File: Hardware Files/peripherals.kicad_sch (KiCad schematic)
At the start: 6 parts, among them J1 Micro_SD_Card_Det1, J2 Conn_ST_STDC14, Y1 16MHz

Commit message: STARTED PCB DESIGN!!
Footprints added to schematic components(some may need to be changed). Organized components and started some rough draft routing. Will most likely need some reorganization, how will parts affect each other(caps, inductors)? NEED TO ADD SOLDER POINTS for battery holder AND FOR 2 other IMUs.
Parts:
- C10, C11: footprint (none) -> Capacitor_SMD:C_Elec_3x5.4
- J1: footprint (none) -> Connector_Card:microSD_HC_Wuerth_693072010801
- J2: footprint (none) -> Connector:Tag-Connect_TC2030-IDC-FP_2x03_P1.27mm_Vertical
- R2: footprint (none) -> Resistor_SMD:R_0201_0603Metric
- Y1: footprint (none) -> Crystal:Crystal_SMD_0603-4Pin_6.0x3.5mm
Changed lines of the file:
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@@
       (effects (font (size 1.27 1.27)) (justify right))
     )
-    (property "Footprint" "" (at 49.53 99.06 0)
+    (property "Footprint" "Connector:Tag-Connect_TC2030-IDC-FP_2x03_P1.27mm_Vertical" (at 49.53 99.06 0)
       (effects (font (size 1.27 1.27)) hide)
     )
@@
       (effects (font (size 1.27 1.27)) (justify left))
     )
-    (property "Footprint" "" (at 53.34 40.64 0)
+    (property "Footprint" "Capacitor_SMD:C_Elec_3x5.4" (at 53.34 40.64 0)
       (effects (font (size 1.27 1.27)) hide)
     )
@@
       (effects (font (size 1.27 1.27)))
     )
-    (property "Footprint" "" (at 64.77 53.34 0)
+    (property "Footprint" "Connector_Card:microSD_HC_Wuerth_693072010801" (at 64.77 53.34 0)
       (effects (font (size 1.27 1.27)) hide)
     )
@@
       (effects (font (size 1.27 1.27)))
     )
-    (property "Footprint" "" (at 43.18 38.1 0)
+    (property "Footprint" "Crystal:Crystal_SMD_0603-4Pin_6.0x3.5mm" (at 43.18 38.1 0)
       (effects (font (size 1.27 1.27)) hide)
     )
@@
       (effects (font (size 1.27 1.27)) (justify left))
     )
-    (property "Footprint" "" (at 53.34 33.02 0)
+    (property "Footprint" "Resistor_SMD:R_0201_0603Metric" (at 53.34 33.02 0)
       (effects (font (size 1.27 1.27)) hide)
     )
@@
       (effects (font (size 1.27 1.27)) (justify left))
     )
-    (property "Footprint" "" (at 33.02 40.64 0)
-      (effects (font (size 1.27 1.27)) hide)
-    )
+    (property "Footprint" "Capacitor_SMD:C_Elec_3x5.4" (at 33.02 40.64 0)
+      (effects (font (size 1.27 1.27)) hide)
+    )

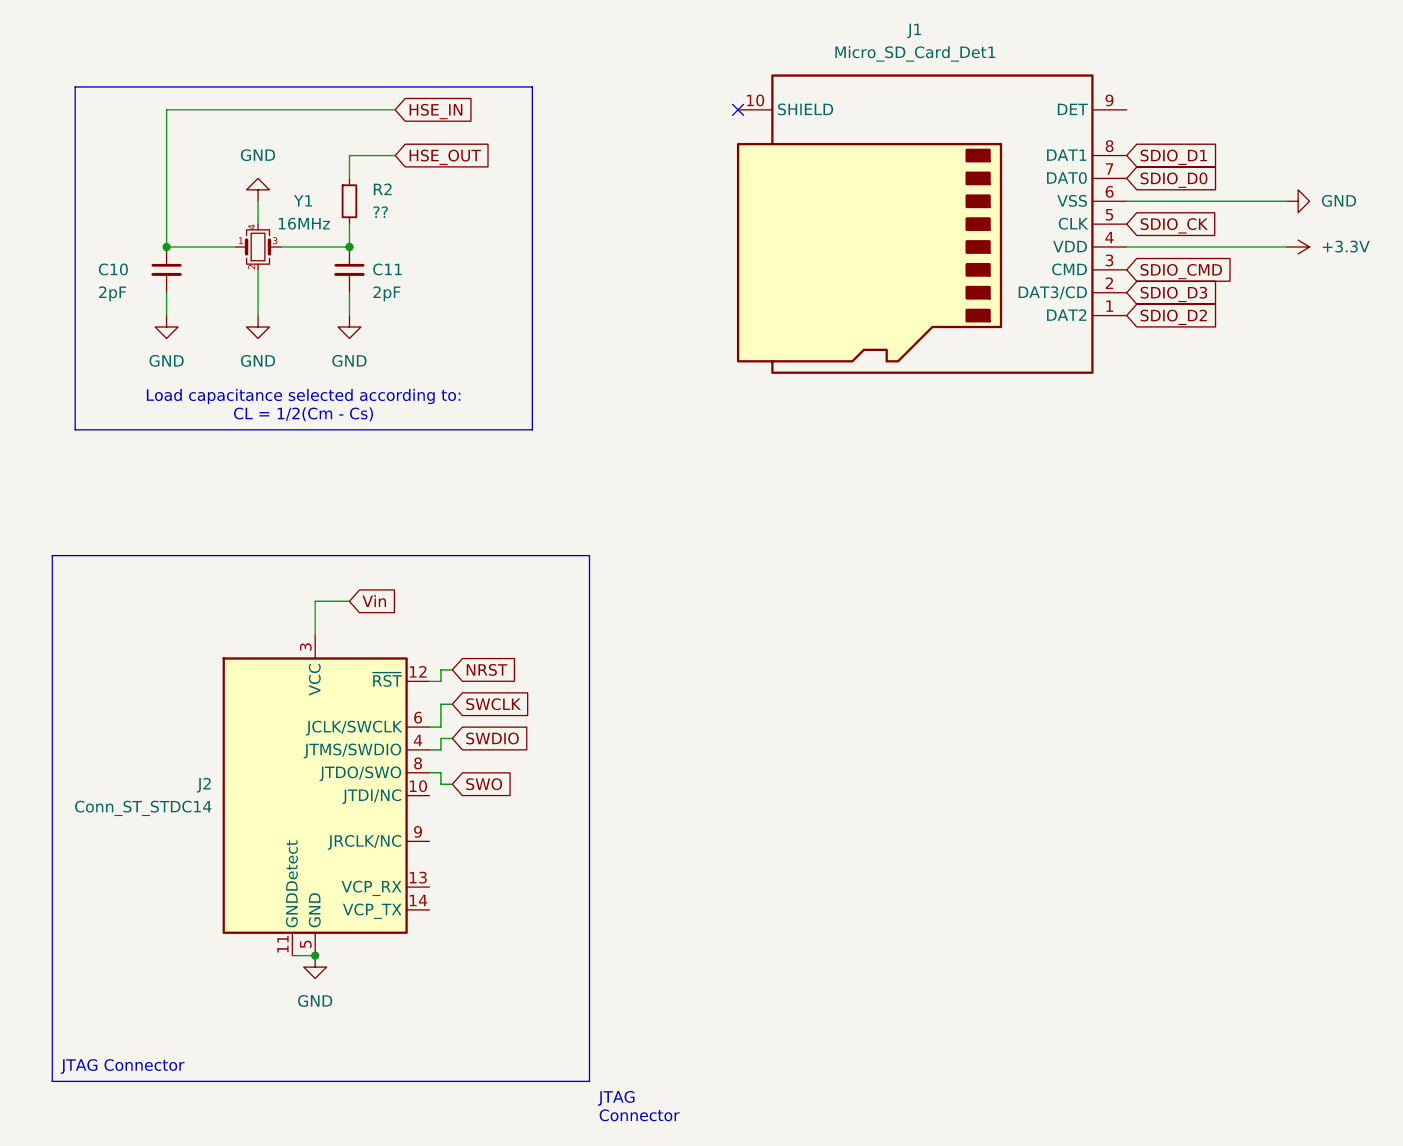
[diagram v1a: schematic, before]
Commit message: Added comments
Added NC flag to the detect pin on SD reader. Left a comment to add NC flags into the MCU for all unused pins.
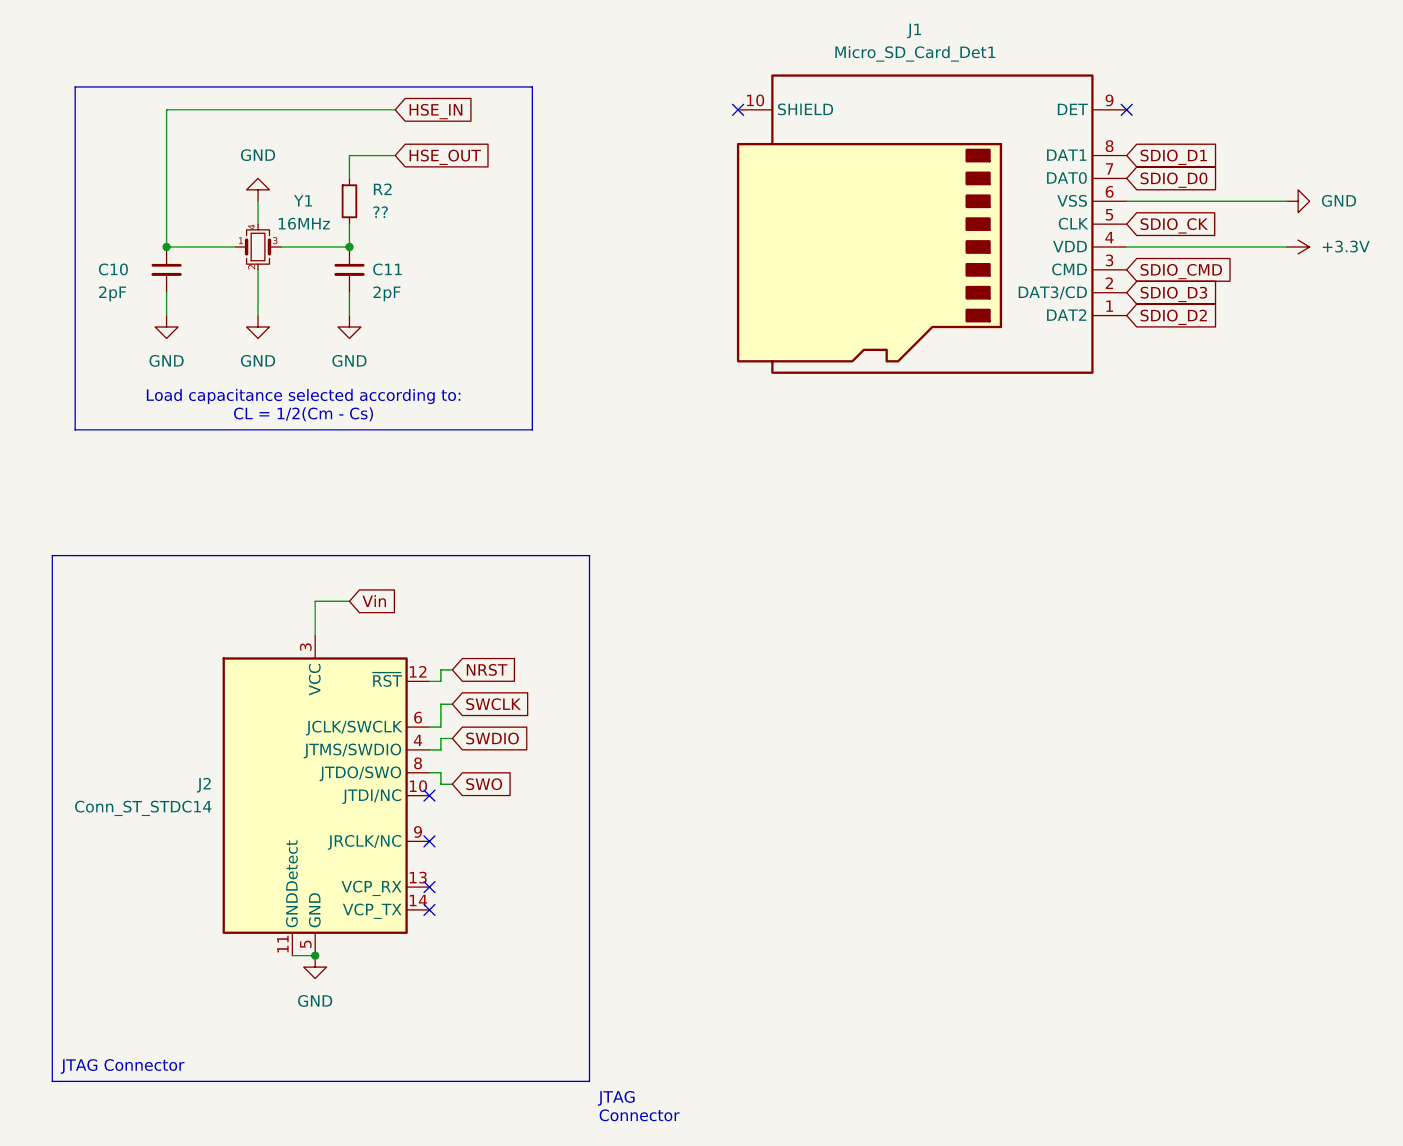
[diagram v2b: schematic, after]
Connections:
- no-connect marks 1 -> 6
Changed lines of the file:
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@@
   )
   (no_connect (at 96.52 22.86))
+  (no_connect (at 62.23 111.76))
+  (no_connect (at 62.23 104.14))
+  (no_connect (at 62.23 109.22))
+  (no_connect (at 139.7 22.86))
+  (no_connect (at 62.23 99.06))
   (wire (pts (xy 43.18 40.64) (xy 43.18 45.72))
     (stroke (width 0) (type default))

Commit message: changed footprints and schematic/pcb setup
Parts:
- C10, C11: footprint Capacitor_SMD:C_Elec_3x5.4 -> Capacitor_SMD:C_0402_1005Metric
- R2: footprint Resistor_SMD:R_0201_0603Metric -> Resistor_SMD:R_0402_1005Metric
- Y1: footprint Crystal:Crystal_SMD_0603-4Pin_6.0x3.5mm -> Crystal:Crystal_SMD_3225-4Pin_3.2x2.5mm
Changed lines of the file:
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@@
       (effects (font (size 1.27 1.27)) (justify left))
     )
-    (property "Footprint" "Capacitor_SMD:C_Elec_3x5.4" (at 53.34 40.64 0)
+    (property "Footprint" "Capacitor_SMD:C_0402_1005Metric" (at 53.34 40.64 0)
       (effects (font (size 1.27 1.27)) hide)
     )
@@
       (effects (font (size 1.27 1.27)))
     )
-    (property "Footprint" "Crystal:Crystal_SMD_0603-4Pin_6.0x3.5mm" (at 43.18 38.1 0)
+    (property "Footprint" "Crystal:Crystal_SMD_3225-4Pin_3.2x2.5mm" (at 43.18 38.1 0)
       (effects (font (size 1.27 1.27)) hide)
     )
@@
       (effects (font (size 1.27 1.27)) (justify left))
     )
-    (property "Footprint" "Resistor_SMD:R_0201_0603Metric" (at 53.34 33.02 0)
+    (property "Footprint" "Resistor_SMD:R_0402_1005Metric" (at 53.34 33.02 0)
       (effects (font (size 1.27 1.27)) hide)
     )
@@
       (effects (font (size 1.27 1.27)) (justify left))
     )
-    (property "Footprint" "Capacitor_SMD:C_Elec_3x5.4" (at 33.02 40.64 0)
-      (effects (font (size 1.27 1.27)) hide)
-    )
+    (property "Footprint" "Capacitor_SMD:C_0402_1005Metric" (at 33.02 40.64 0)
+      (effects (font (size 1.27 1.27)) hide)
+    )

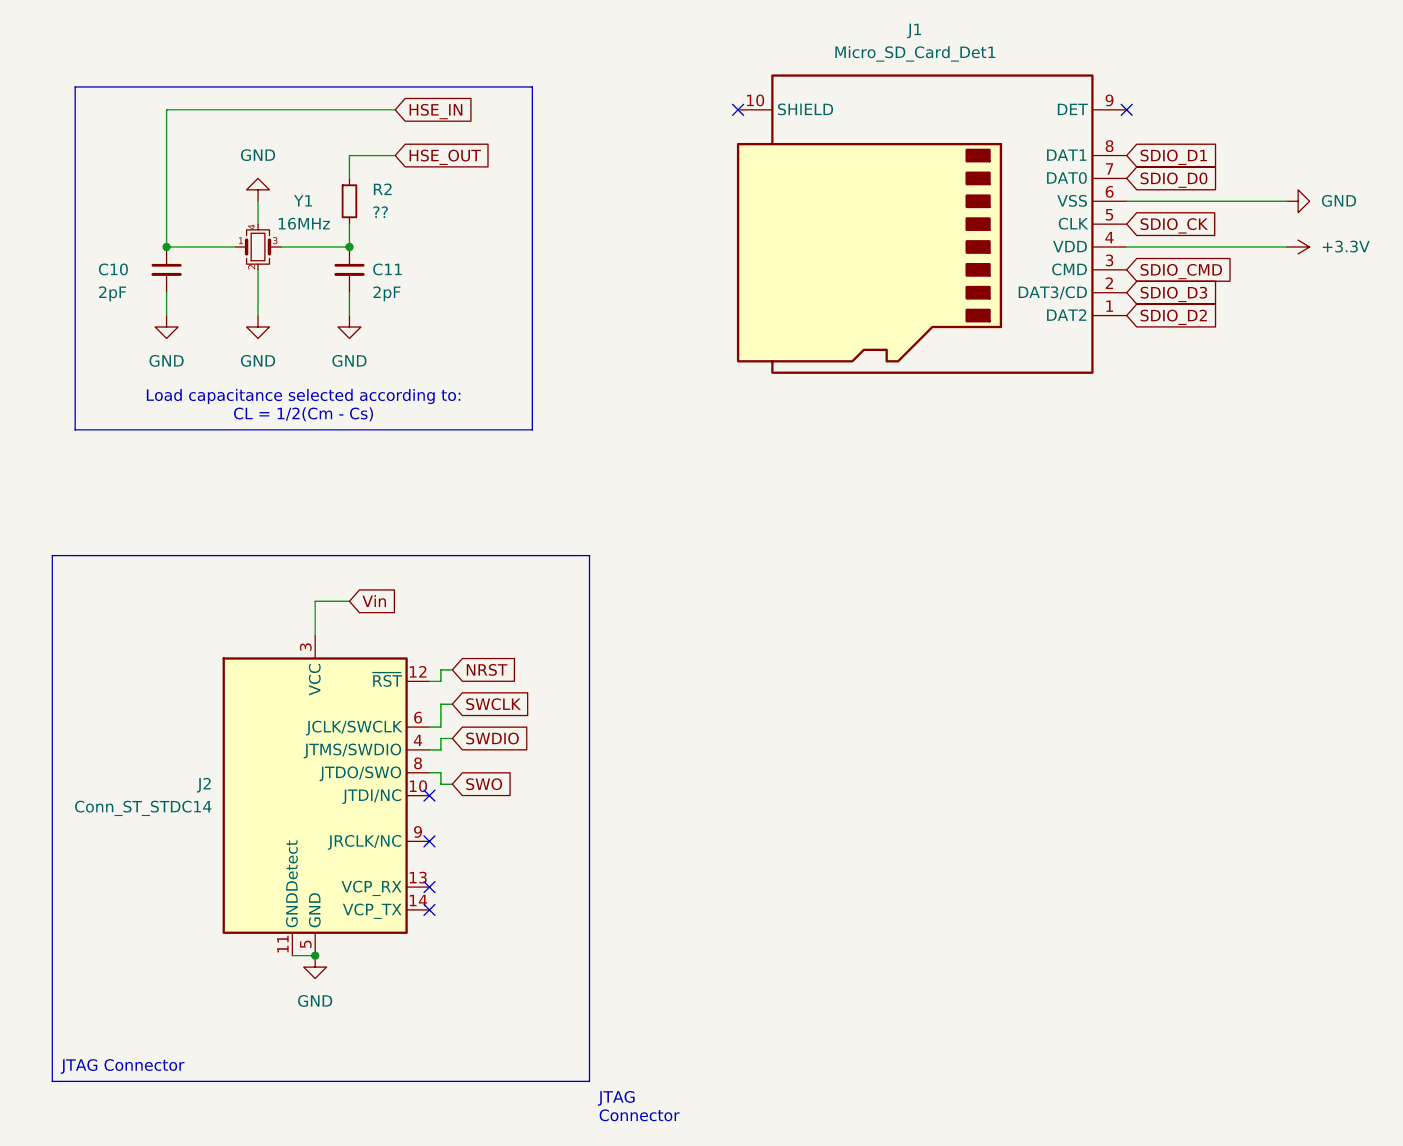
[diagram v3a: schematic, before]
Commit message: added pinouts for other imus and battery supply. Almost finished layout of pcb, routing next week
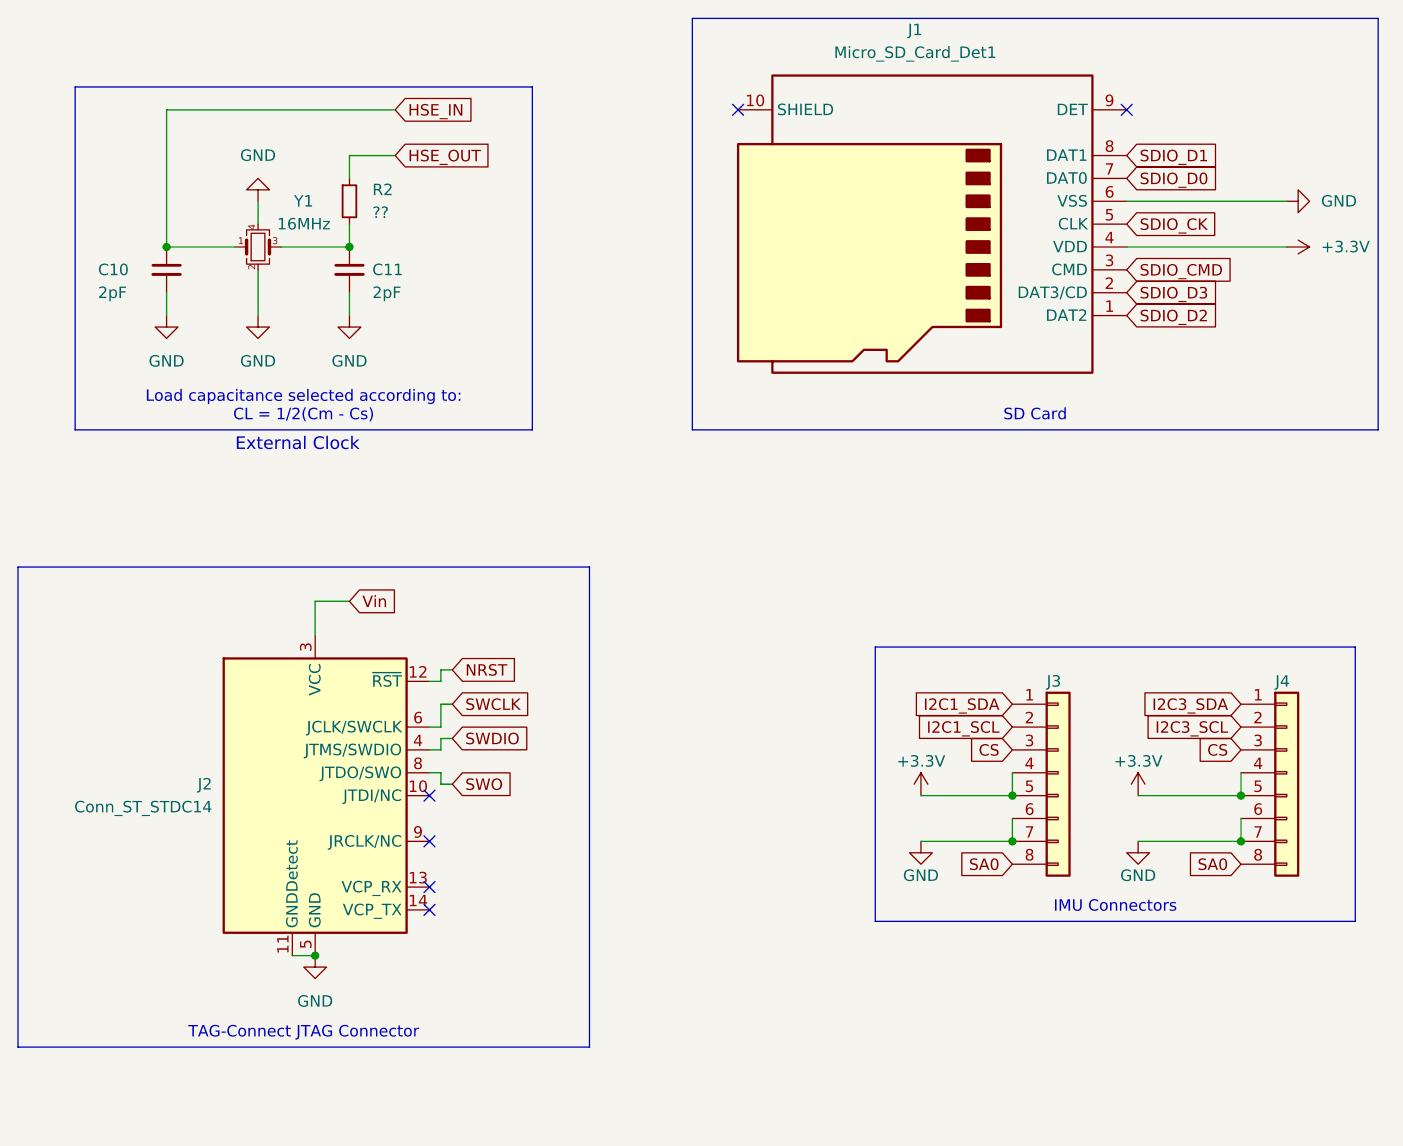
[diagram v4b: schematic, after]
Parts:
- added J3, J4: Conn_01x08, Connector_PinSocket_1.00mm:PinSocket_1x08_P1.00mm_Vertical_SMD_Pin1Left, symbol Connector_Generic:Conn_01x08
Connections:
- net +3.3V: now also J3.4 (Pin_4), J3.5 (Pin_5), J4.4 (Pin_4), J4.5 (Pin_5)
- net GND: now also J3.6 (Pin_6), J3.7 (Pin_7), J4.6 (Pin_6), J4.7 (Pin_7)
- new net CS: J3.3 (Pin_3), J4.3 (Pin_3)
- new net I2C1_SCL: J3.2 (Pin_2)
- new net I2C1_SDA: J3.1 (Pin_1)
- new net I2C3_SCL: J4.2 (Pin_2)
- new net I2C3_SDA: J4.1 (Pin_1)
- new net SA0: J3.8 (Pin_8), J4.8 (Pin_8)
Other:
- note added: "External Clock"
